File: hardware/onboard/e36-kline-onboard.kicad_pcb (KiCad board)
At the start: 2 copper layers, 90 x 50 mm, 43 parts, among them J1 OBD2-M-90, J2 DEBUG, J3 USB-C 16P, J4 PIGTAIL, SW1 RESET, SW2 BOOT, U1 L9637D, U2 AP63203, U3 ESP32-S3-WROOM-1-N16R8

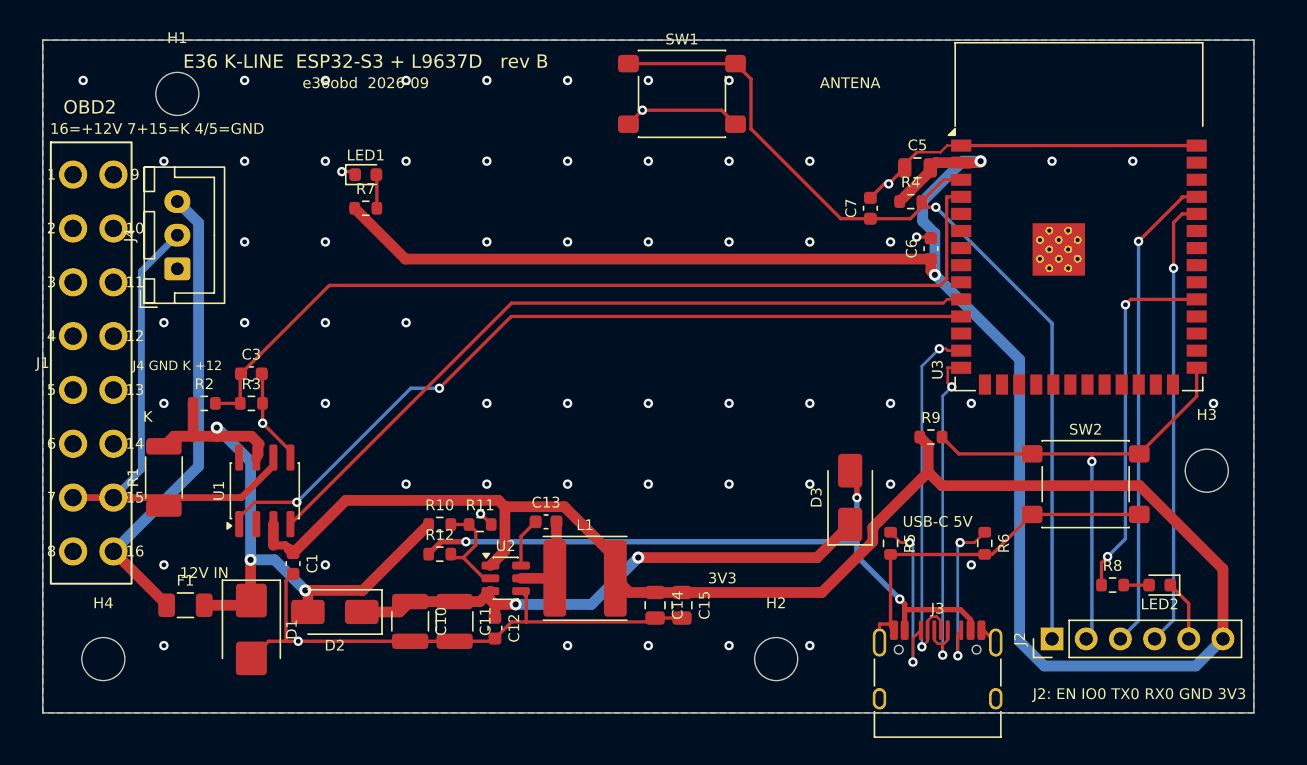
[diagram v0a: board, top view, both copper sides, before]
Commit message: hardware: onboard case restyle, M50 badge, USB-C capture, pigtail variant
- Case: R6 corners, 45-degree chamfers, seam shadow line, brass M3 heat-set
  inserts (M3x12 from below), O3 light pipes for the LEDs, clip holes for
  RESET/BOOT, OBD2 plug modelled with its D profile.
- Badge as a separate part: 85x22 black field, 13 silver ribs at 1.6 mm pitch
  running the lid, BMW plaque off-centre cutting only the middle ribs
  (filament change at 1.6 mm), copied from the M50 valve cover.
- USB-C receptacle protrudes 1.6 mm and passes through a shell-shaped opening
  flush with a bezel; board grown to 90x50, shelf under the board edge.
- J4 JST-XH pigtail (GND/K/+12) to go direct to the 20-pin round connector;
  pin 16 (KL15) powers the board only with ignition. CASE_PIGTAIL=1 variant.
- Buck UVLO on EN (on 12.5 V / off 11.5 V, USB overrides). BOOT and status LED
  relocated to clear the badge band. DRC 0 errors, 0 unconnected.
- EEVEE renders with lights; READMEs updated.

Co-Authored-By: Claude Fable 5.1 <noreply@anthropic.com>
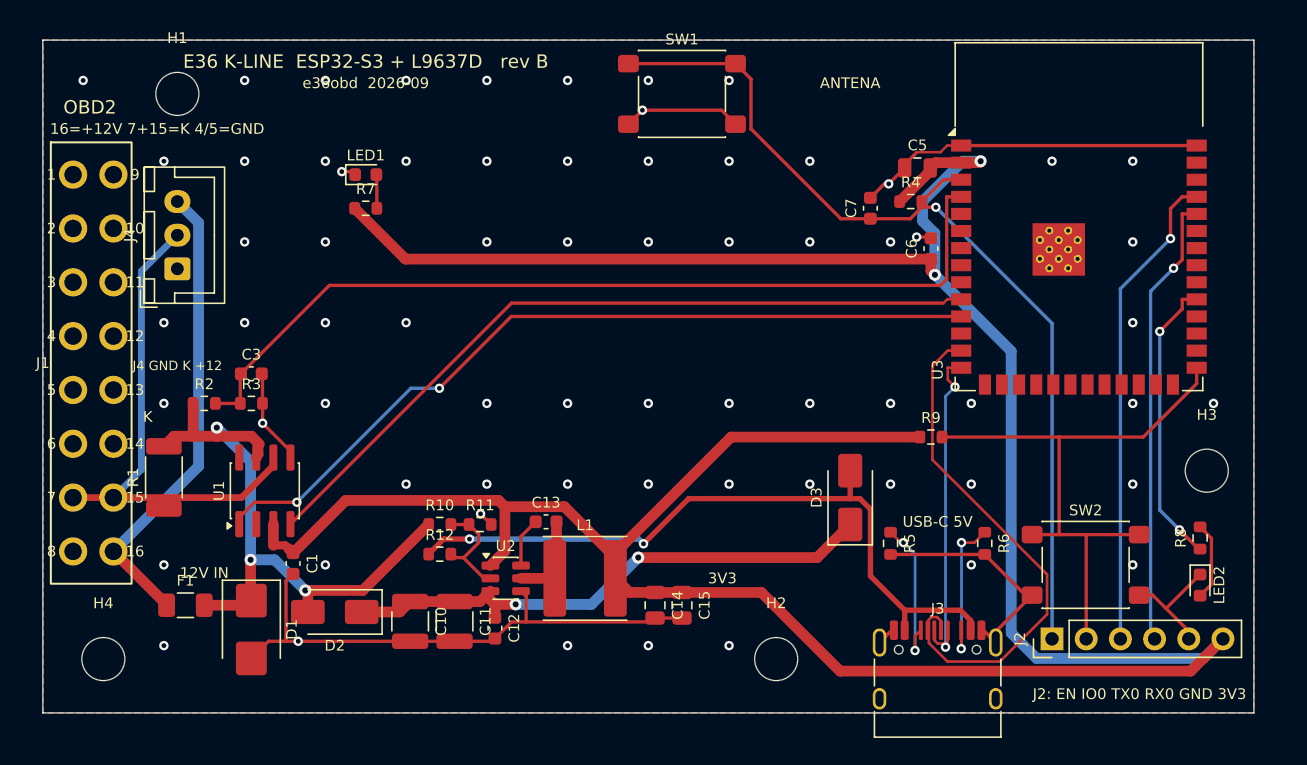
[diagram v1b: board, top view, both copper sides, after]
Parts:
- moved R8 7.38 mm to (106.0, 57.0), turned to 90 degrees
- moved SW2 6.00 mm to (97.5, 59.0)
- moved LED2 3.00 mm to (106.0, 60.5), turned to -90 degrees
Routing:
- net +3V3: track 208.9 -> 223.0 mm
- net USB_DN: track 28.4 -> 39.0 mm, vias 2 -> 0
- net IO0: track 37.3 -> 44.7 mm, vias 1 -> 0
- net GND: track 120.5 -> 114.9 mm, vias 63 -> 68
- net IO38: track 27.0 -> 21.6 mm
- net LED2_A: track 1.89 -> 5.81 mm
- net CC1: track 13.3 -> 11.3 mm
- net VBUS: track 51.7 -> 53.2 mm, vias 3 -> 2
- net CC2: track 12.6 -> 11.3 mm
- net USB_DP: track 26.3 -> 25.3 mm

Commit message: hardware: verified LCSC codes, JLCPCB/PCBWay pricing, PCBWay sample package; archive session
- BOM: three wrong LCSC codes found while pricing and fixed (L9637D -> C153038
  E-L9637D013TR, 3.74k -> C23016, LEDs -> basic 0603 KT-0603W/R), plus verified
  codes for TVS, 2010 pull-up, 50 V input caps, 36k; gerbers/BOM/CPL regenerated
  (DRC 0 errors, 0 unconnected). BOOT button and status LED relocated to clear the
  badge band; badge now 13 ribs with continuous outer ribs past the BMW plaque.
- pricing.py: JLCPCB estimate from their parts API + published fees
  (~97 USD / 5 boards, ~140 / 10). pcbway.py: PCBWay one-sample package (BOM in
  their format with MPNs, centroids, drawing, order notes) and the official quote
  from PCBWay's quote engine (PCB 6.50, assembly 88 flat, shipping 48.87-72.73).
- sessions/: archive this Claude Code session transcript.

Co-Authored-By: Claude Fable 5.1 <noreply@anthropic.com>
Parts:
- F1: value 1A 63V -> 1A 32V
- LED1: value PWR verde -> PWR blanco
- LED2: value STATUS ambar -> STATUS rojo
